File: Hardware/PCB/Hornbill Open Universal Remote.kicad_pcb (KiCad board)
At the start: 2 copper layers, 93 x 60 mm, 66 parts, among them CON1 USB-MINI-B, M1 ESP-WROOM-32, P1 CONN_01X14, P10 CONN_01X14, P11 CONN_01X14, P12 CONN_01X14, P13 CONN_01X14, P14 CONN_01X14, P15 CONN_01X14, P2 CONN_01X03, P3 CONN_01X14, P4 CONN_01X14, P5 CONN_01X14, P6 CONN_01X14, P7 CONN_01X14, P8 CONN_01X14, P9 CONN_01X14, Q1 IRLML5203, Q2 Q_NPN_BEC, Q3 S8050, Q4 S8050, SW1 SW_PUSH, SW2 SW_PUSH, U1 AP2112K, U2 OSH_Symbol, U3 EE_Logo, U4 EE_Logo, U5 MountingHole, U6 MountingHole, U7 MountingHole, U8 MountingHole, U9 CP2104, Y1 32.768KHz RTC Crystal

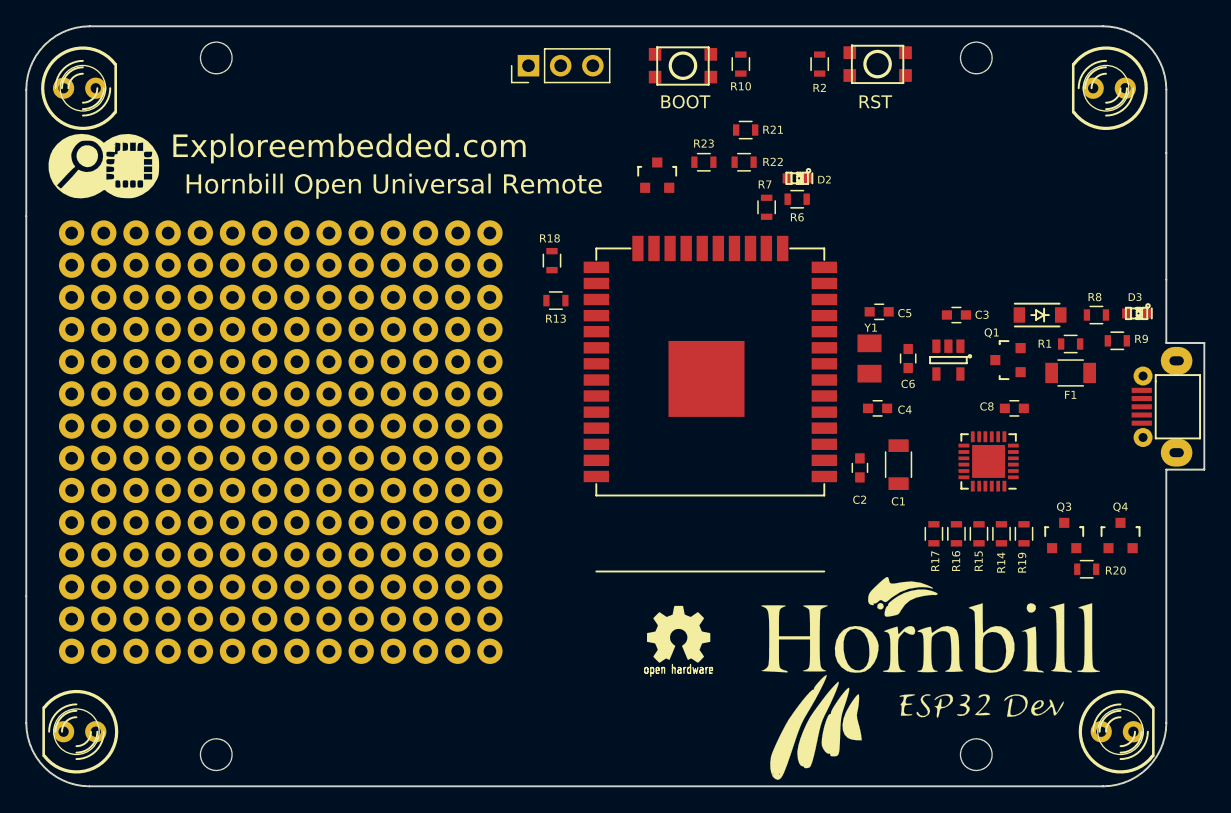
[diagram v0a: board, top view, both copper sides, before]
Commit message: Hornbill logo added for OUR
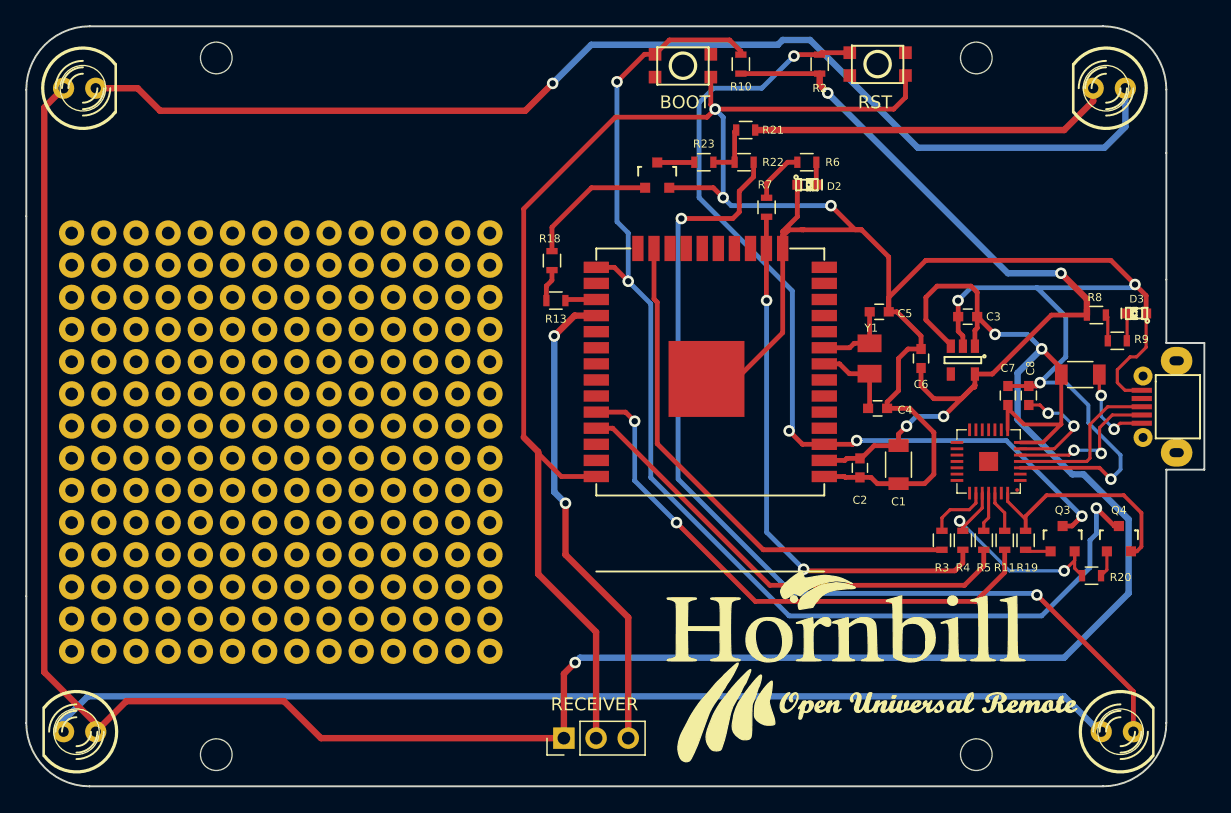
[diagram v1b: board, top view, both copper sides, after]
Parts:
- removed D1: BAT20J, Explore:SOD-80_diode
- removed Q1: IRLML5203, Explore:SOT-23
- removed R1: 100K, Resistors_SMD:R_0603
- removed R14, R15, R16, R17: 0E, Resistors_SMD:R_0603
- removed U3: EE_Logo, Logo:Hornbill
- added C7: 0.1uF, Capacitors_SMD:C_0603, F.Cu at (142.5, 96.6)
- added G***: LOGO, OUR logo:our, F.Cu at (131.7, 118.0)
- added R11: 0E, Resistors_SMD:R_0603, F.Cu at (142.2, 108.1)
- added R3: 0E, Resistors_SMD:R_0603, F.Cu at (137.3, 108.1)
- added R4: 0E, Resistors_SMD:R_0603, F.Cu at (138.9, 108.1)
- added R5: 0E, Resistors_SMD:R_0603, F.Cu at (140.6, 108.1)
- C8: value 10uF -> 0.1uF
- F1: footprint Capacitors_SMD:C_1206 -> Explore:Fuse_500mA
- U2, U4: moved to B.Cu
- U9: value CP2104 -> CP2102; footprint Explore:CP2104 -> Explore:cp2102_xl2
- moved U4 77.1 mm to (145.8, 97.4), turned to 180 degrees
- moved P2 53.2 mm to (107.4, 123.7)
- moved U2 25.0 mm to (92.6, 122.7), turned to 180 degrees
- moved R6 3.02 mm to (126.6, 78.2)
- moved C8 1.53 mm to (144.1, 96.6), turned to 90 degrees
- moved U1 1.14 mm to (138.9, 93.9)
- moved C6 1.02 mm to (135.6, 93.7)
- moved D2 0.92 mm to (126.6, 80.0)
- moved C3 0.90 mm to (139.3, 90.4)
- moved F1 0.77 mm to (148.2, 95.0), turned to 0 degrees
- moved R20 0.63 mm to (149.1, 110.9)
- moved R19 0.52 mm to (143.9, 108.1)
- moved Q3 0.28 mm to (146.8, 108.0)
- moved Q4 0.28 mm to (151.3, 108.0)
- turned D3 to 180 degrees
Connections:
- C8 pad 1: GND -> Net-(C8-Pad1)
- C8 pad 2: +3V3 -> GND
- F1 pad 1: Net-(CON1-Pad1) -> +5V
- F1 pad 2: VCC -> Net-(CON1-Pad1)
- U9 pad 19: /RTS -> (no net)
- U9 pad 2: GND -> Net-(U9-Pad2)
- U9 pad 23: /DTR -> Net-(R3-Pad2)
- U9 pad 24: Net-(U9-Pad24) -> /RTS
- U9 pad 25: GND -> Net-(R5-Pad2)
- U9 pad 3: Net-(CON1-Pad3) -> GND
- U9 pad 4: Net-(CON1-Pad2) -> Net-(CON1-Pad3)
- U9 pad 5: +3V3 -> Net-(CON1-Pad2)
- U9 pad 6: +3V3 -> Net-(C8-Pad1)
- U9 pad 7: +3V3 -> +5V
- U9 pad 8: VCC -> +5V
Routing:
- net GND: track 0.00 -> 257.4 mm, vias 0 -> 7
- net +5V: track 0.00 -> 206.0 mm, vias 0 -> 3
- net /IO0: track 0.00 -> 95.2 mm, vias 0 -> 3
- net Net-(D5-Pad2): track 0.00 -> 91.6 mm, vias 0 -> 1
- net Net-(D10-Pad1): track 0.00 -> 84.8 mm
- net Net-(D10-Pad2): track 0.00 -> 75.9 mm, vias 0 -> 2
- net /EN: track 0.00 -> 70.6 mm, vias 0 -> 4
- net +3V3: track 0.00 -> 69.9 mm, vias 0 -> 4
- net /RXD0: track 0.00 -> 43.9 mm, vias 0 -> 2
- net /IO13: track 0.00 -> 43.0 mm, vias 0 -> 2
- net /IO15: track 0.00 -> 41.5 mm
- net /IR_Rx: track 0.00 -> 38.2 mm, vias 0 -> 2
- net /TXD0: track 0.00 -> 37.6 mm
- net Net-(D9-Pad2): track 0.00 -> 28.6 mm
- net /DTR: track 0.00 -> 18.8 mm
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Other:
- board text added: "RECEIVER"
- board text removed: "Hornbill Open Universal Remote"

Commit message: IO pins taken out
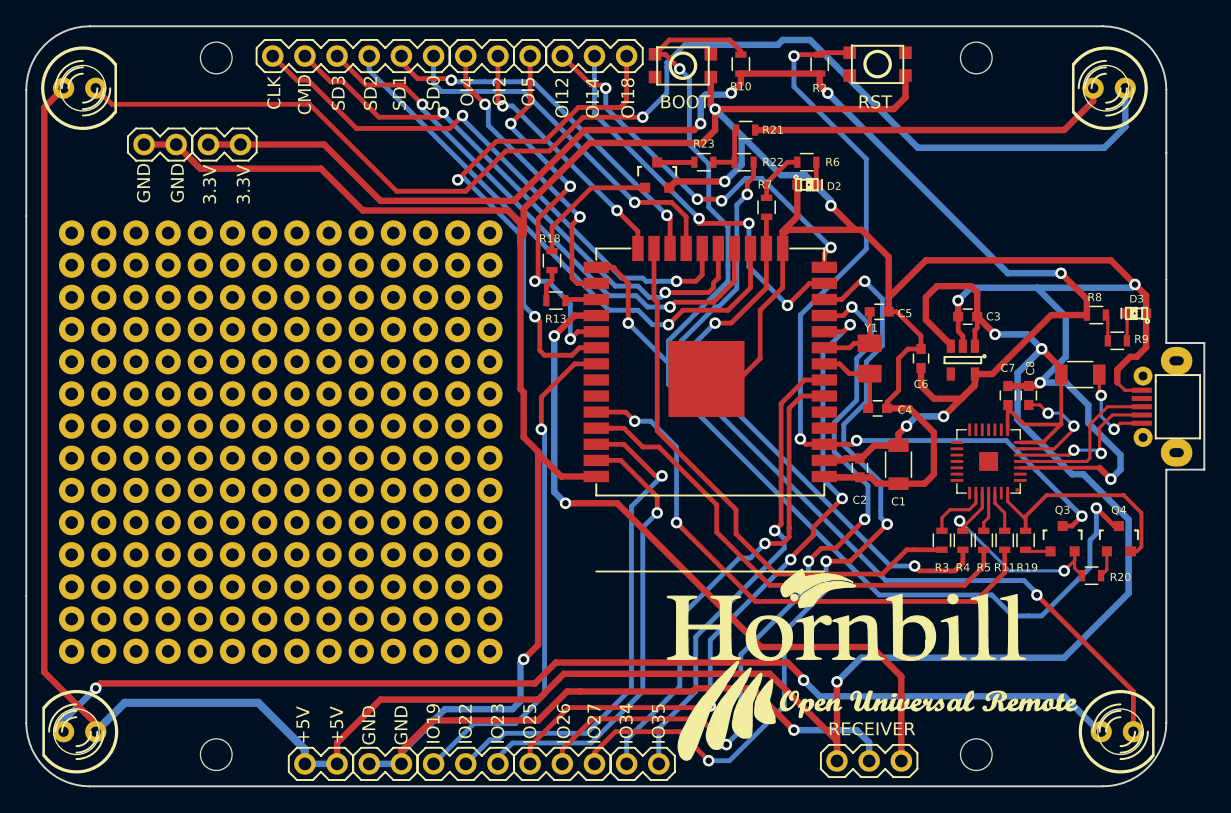
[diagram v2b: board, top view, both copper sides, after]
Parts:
- removed G***: LOGO, OUR logo:our
- added P16: CONN_01X02, Pin_Headers:Pin_Header_Straight_1x02_Pitch2.54mm, F.Cu at (99.7, 69.8)
- added P17: CONN_01X03, Pin_Headers:Pin_Header_Straight_1x03_Pitch2.54mm, F.Cu at (112.4, 69.8)
- added P18: CONN_01X03, Pin_Headers:Pin_Header_Straight_1x03_Pitch2.54mm, F.Cu at (102.2, 125.7)
- added P19: CONN_01X03, Pin_Headers:Pin_Header_Straight_1x03_Pitch2.54mm, F.Cu at (109.9, 125.7)
- added P20: CONN_01X01, Pin_Headers:Pin_Header_Straight_1x01_Pitch2.54mm, F.Cu at (104.8, 69.8)
- added P21: CONN_01X02, Pin_Headers:Pin_Header_Straight_2x01_Pitch2.54mm, F.Cu at (79.4, 76.8)
- added P22: CONN_01X02, Pin_Headers:Pin_Header_Straight_2x01_Pitch2.54mm, F.Cu at (87.0, 125.7)
- added P23: CONN_01X06, Pin_Headers:Pin_Header_Straight_1x06_Pitch2.54mm, F.Cu at (97.2, 69.8)
- added P24: CONN_01X02, Pin_Headers:Pin_Header_Straight_1x02_Pitch2.54mm, F.Cu at (114.9, 125.7)
- added P25: CONN_01X02, Pin_Headers:Pin_Header_Straight_1x02_Pitch2.54mm, F.Cu at (74.3, 76.8)
- added P26: CONN_01X02, Pin_Headers:Pin_Header_Straight_1x02_Pitch2.54mm, F.Cu at (92.1, 125.7)
- added U3: EE_Logo, Logo:Hornbill_OUR, F.Cu at (131.7, 117.9)
- moved U2 59.2 mm to (151.2, 114.8)
- moved P2 21.6 mm to (129.0, 125.5)
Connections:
- M1 pad 10: Net-(M1-Pad10) -> /IO25
- M1 pad 11: Net-(M1-Pad11) -> /IO26
- M1 pad 12: Net-(M1-Pad12) -> /IO27
- M1 pad 13: Net-(M1-Pad13) -> /IO14
- M1 pad 14: Net-(M1-Pad14) -> /IO12
- M1 pad 17: Net-(M1-Pad17) -> /SD2
- M1 pad 18: Net-(M1-Pad18) -> /SD3
- M1 pad 19: Net-(M1-Pad19) -> /CMD
- M1 pad 20: Net-(M1-Pad20) -> /CLK
- M1 pad 21: Net-(M1-Pad21) -> /SD0
- M1 pad 22: Net-(M1-Pad22) -> /SD1
- M1 pad 24: Net-(M1-Pad24) -> /IO2
- M1 pad 26: Net-(M1-Pad26) -> /IO4
- M1 pad 29: Net-(M1-Pad29) -> /IO5
- M1 pad 30: Net-(M1-Pad30) -> /IO18
- M1 pad 31: Net-(M1-Pad31) -> /IO19
- M1 pad 36: Net-(M1-Pad36) -> /IO22
- M1 pad 37: Net-(M1-Pad37) -> /IO23
- M1 pad 6: Net-(M1-Pad6) -> /IO34
- M1 pad 7: Net-(M1-Pad7) -> /IO35
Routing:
- net GND: track 257.4 -> 357.0 mm, vias 7 -> 9
- net /IO27: track 0.00 -> 64.4 mm, vias 0 -> 4
- net /IO26: track 0.00 -> 61.2 mm, vias 0 -> 4
- net /IO25: track 0.00 -> 55.2 mm, vias 0 -> 4
- net +3V3: track 69.9 -> 119.5 mm, vias 4 -> 6
- net /CLK: track 0.00 -> 44.6 mm, vias 0 -> 2
- net /CMD: track 0.00 -> 44.1 mm, vias 0 -> 2
- net /SD2: track 0.00 -> 43.9 mm, vias 0 -> 1
- net /SD3: track 0.00 -> 43.2 mm, vias 0 -> 2
- net /IO18: track 0.00 -> 41.0 mm, vias 0 -> 2
- net /IO19: track 0.00 -> 40.0 mm, vias 0 -> 1
- net /IO22: track 0.00 -> 39.5 mm, vias 0 -> 1
- net /IO34: track 0.00 -> 38.0 mm, vias 0 -> 1
- net /IO35: track 0.00 -> 37.3 mm, vias 0 -> 1
- net /IO23: track 0.00 -> 35.9 mm, vias 0 -> 1
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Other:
- board text added: "+5V"
- board text added: "3.3V"
- board text added: "CLK"
- board text added: "CMD"
- board text added: "GND"
- board text added: "IO19"
- board text added: "IO22"
- board text added: "IO23"
- board text added: "IO25"
- board text added: "IO26"
- board text added: "IO27"
- board text added: "IO34"
- board text added: "IO35"
- board text added: "OI12"
- board text added: "OI14"
- board text added: "OI18"
- board text added: "OI2"
- board text added: "OI4"
- board text added: "OI5"
- board text added: "SD0"
- board text added: "SD1"
- board text added: "SD2"
- board text added: "SD3"

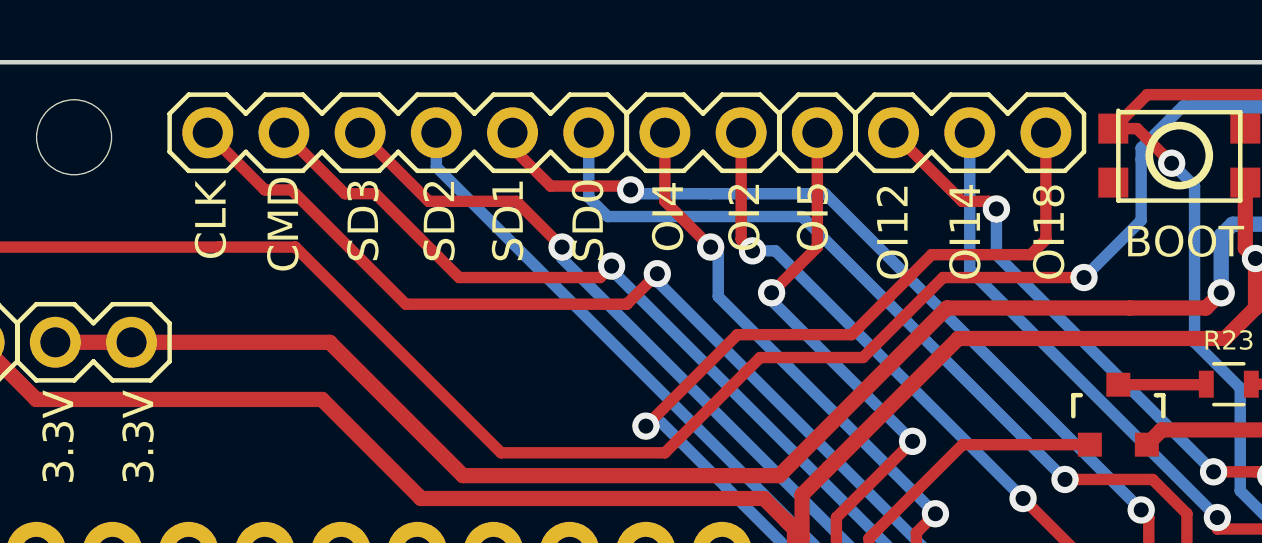
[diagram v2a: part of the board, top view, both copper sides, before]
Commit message: PCB legends renamed and gerber file generated
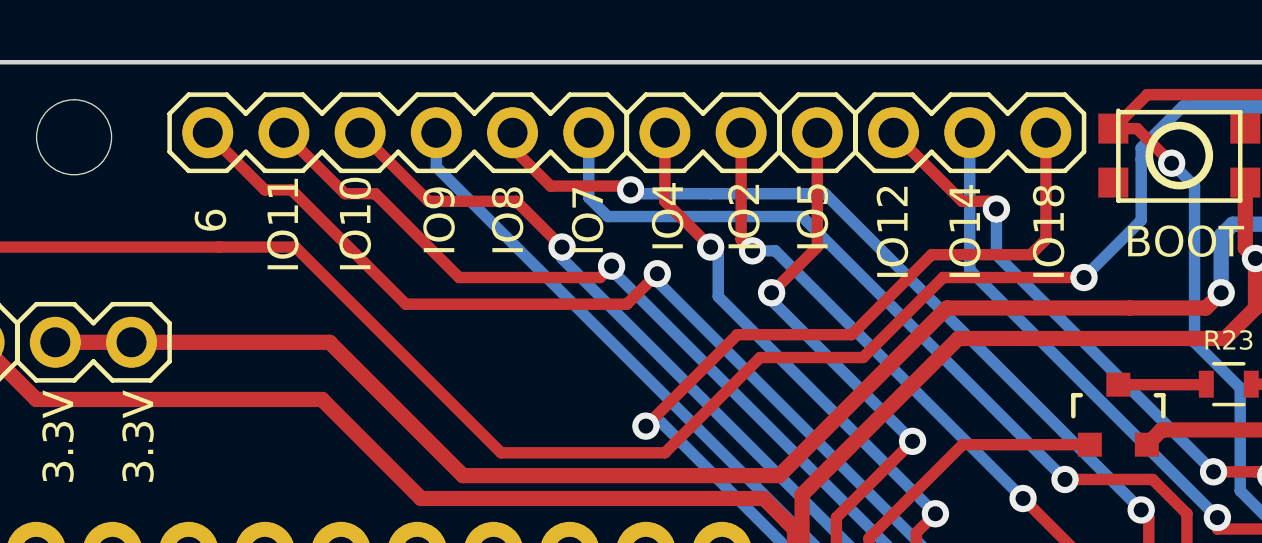
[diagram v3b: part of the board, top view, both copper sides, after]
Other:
- board text added: "6"
- board text added: "IO10"
- board text added: "IO11"
- board text added: "IO12"
- board text added: "IO14"
- board text added: "IO18"
- board text added: "IO2"
- board text added: "IO4"
- board text added: "IO5"
- board text added: "IO7"
- board text added: "IO8"
- board text added: "IO9"
- board text added: "v1.0"
- board text removed: "CLK"
- board text removed: "CMD"
- board text removed: "OI12"
- board text removed: "OI14"
- board text removed: "OI18"
- board text removed: "OI2"
- board text removed: "OI4"
- board text removed: "OI5"
- board text removed: "SD0"
- board text removed: "SD1"
- board text removed: "SD2"
- board text removed: "SD3"
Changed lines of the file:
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@@
-(kicad_pcb (version 4) (host pcbnew 4.0.5)
+(kicad_pcb (version 4) (host pcbnew 4.0.7)
   (general
     (links 108)
@@
     (area 64.924999 67.424999 158.075001 127.575001)
     (thickness 1.6)
-    (drawings 60)
+    (drawings 61)
     (tracks 828)
     (zones 0)
@@
   )
   (setup
-    (last_trace_width 0.508)
+    (last_trace_width 0.25)
     (user_trace_width 0.3048)
     (user_trace_width 0.381)
@@
       (xy -1.633999 -6.578827) (xy -1.4478 -6.474278) (xy -1.4478 -6.474278)) (layer F.SilkS) (width 0.1))
   )
-  (gr_text OI18 (at 112.522 73.152 90) (layer F.SilkS)
+  (gr_text v1.0 (at 143.256 81.534) (layer B.SilkS)
+    (effects (font (size 1.016 1.016) (thickness 0.254)) (justify mirror))
+  )
+  (gr_text IO18 (at 112.522 73.152 90) (layer F.SilkS)
     (effects (font (size 1.016 1.016) (thickness 0.254)))
   )
-  (gr_text OI14 (at 109.728 73.152 90) (layer F.SilkS)
+  (gr_text IO14 (at 109.728 73.152 90) (layer F.SilkS)
     (effects (font (size 1.016 1.016) (thickness 0.254)))
   )
-  (gr_text OI12 (at 107.315 73.152 90) (layer F.SilkS)
+  (gr_text IO12 (at 107.315 73.152 90) (layer F.SilkS)
     (effects (font (size 1.016 1.016) (thickness 0.254)))
   )
-  (gr_text OI5 (at 104.648 72.644 90) (layer F.SilkS)
+  (gr_text IO5 (at 104.648 72.644 90) (layer F.SilkS)
     (effects (font (size 1.016 1.016) (thickness 0.254)))
   )
-  (gr_text OI2 (at 102.362 72.644 90) (layer F.SilkS)
+  (gr_text IO2 (at 102.362 72.644 90) (layer F.SilkS)
     (effects (font (size 1.016 1.016) (thickness 0.254)))
   )
-  (gr_text OI4 (at 99.822 72.644 90) (layer F.SilkS)
+  (gr_text IO4 (at 99.822 72.644 90) (layer F.SilkS)
     (effects (font (size 1.016 1.016) (thickness 0.254)))
   )
-  (gr_text SD0 (at 97.155 72.771 90) (layer F.SilkS)
+  (gr_text IO7 (at 97.155 72.771 90) (layer F.SilkS)
     (effects (font (size 1.016 1.016) (thickness 0.254)))
   )
-  (gr_text SD2 (at 92.202 72.771 90) (layer F.SilkS)
+  (gr_text IO9 (at 92.202 72.771 90) (layer F.SilkS)
     (effects (font (size 1.016 1.016) (thickness 0.254)))
   )
-  (gr_text SD1 (at 94.488 72.771 90) (layer F.SilkS)
+  (gr_text IO8 (at 94.488 72.771 90) (layer F.SilkS)
     (effects (font (size 1.016 1.016) (thickness 0.254)))
   )
-  (gr_text SD3 (at 89.662 72.771 90) (layer F.SilkS)
+  (gr_text IO10 (at 89.408 72.898 90) (layer F.SilkS)
     (effects (font (size 1.016 1.016) (thickness 0.254)))
   )
-  (gr_text CMD (at 86.995 72.898 90) (layer F.SilkS)
+  (gr_text IO11 (at 86.995 72.898 90) (layer F.SilkS)
     (effects (font (size 1.016 1.016) (thickness 0.254)))
   )
-  (gr_text CLK (at 84.582 72.771 90) (layer F.SilkS)
+  (gr_text 6 (at 84.582 72.771 90) (layer F.SilkS)
     (effects (font (size 1.016 1.016) (thickness 0.254)))
   )
